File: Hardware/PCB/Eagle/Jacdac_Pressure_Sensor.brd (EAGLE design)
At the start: 27.9 x 27.9 mm, 29 parts, among them J1 JACDAC_EDGE_CONN-INNIE, J2 SWD-ADAPTER-, U1 NCP114ASN330T1G, U2 STM32F042F6P6, U3 LPS33HWTR, U4 BAT54S,235

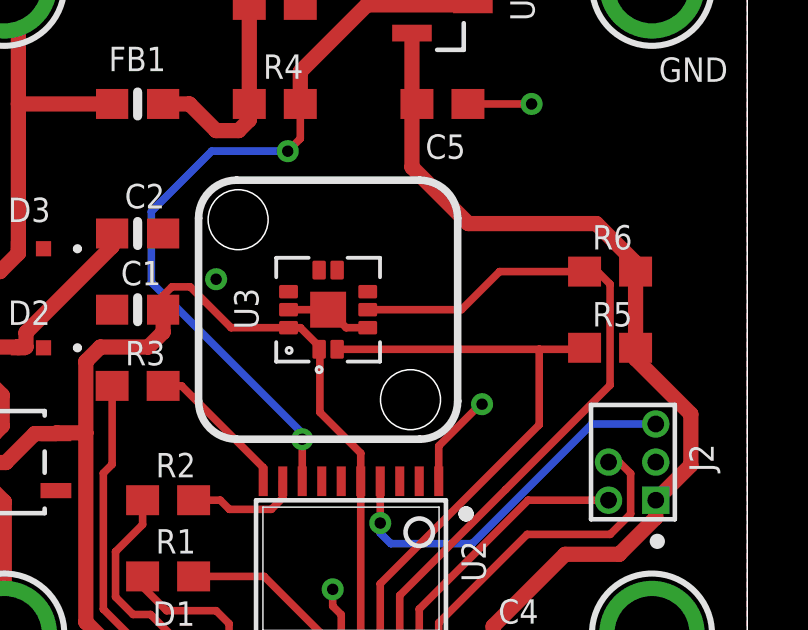
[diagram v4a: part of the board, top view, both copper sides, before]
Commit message: Added Additional ground via
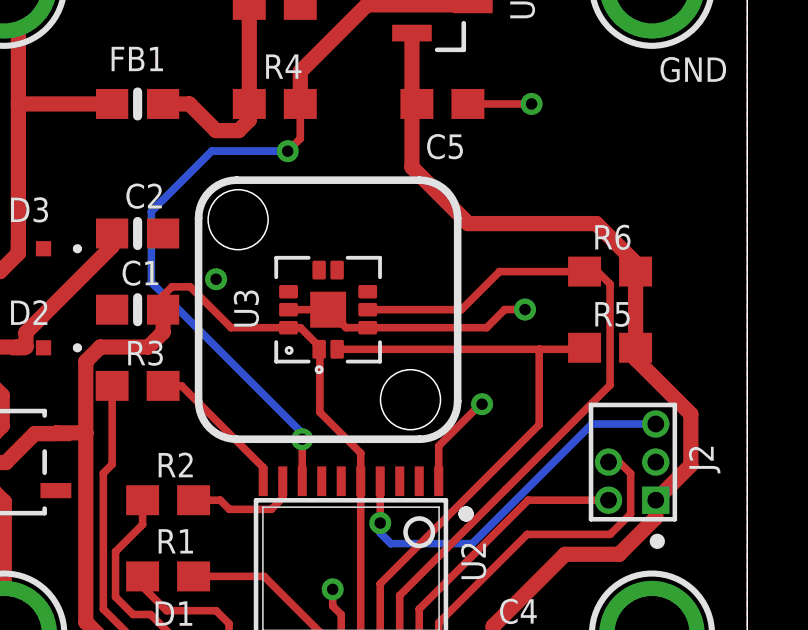
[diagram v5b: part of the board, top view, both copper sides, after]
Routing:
- net GND: track 15.9 -> 21.4 mm, vias 5 -> 6
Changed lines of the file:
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@@
 <drawing>
 <settings>
-<setting alwaysvectorfont="yes"/>
+<setting alwaysvectorfont="no"/>
 <setting keepoldvectorfont="yes"/>
 <setting verticaltext="up"/>
@@
 </layers>
 <board>
-<fusionsync huburn="a.cGVyc29uYWw6dWUyYWQxOTI2" projecturn="a.cGVyc29uYWw6dWUyYWQxOTI2IzIwMjEwOTEzNDQzNTc2ODA2" f3durn="urn:adsk.wipprod:dm.lineage:uby1OiGsR5OmPWsZuNtneA" pcbguid="" lastpulledtime="" lastsyncedchangeguid="" latestrevisionid="af606afd-fa91-40a1-9cdc-3a86e01ece8c" lastsyncedrevisionid="af606afd-fa91-40a1-9cdc-3a86e01ece8c" lastboardhashguid="dc86e965-abde-f830-b550-b611301090e1" lastpushedtime="2022-03-29T02:43:38Z" linktopcb3d="true"/>
+<fusionsync huburn="a.cGVyc29uYWw6dWUyYWQxOTI2" projecturn="a.cGVyc29uYWw6dWUyYWQxOTI2IzIwMjEwOTEzNDQzNTc2ODA2" f3durn="urn:adsk.wipprod:dm.lineage:uby1OiGsR5OmPWsZuNtneA" pcbguid="" lastpulledtime="" lastsyncedchangeguid="" latestrevisionid="1d99499d-ddfe-4265-9c5c-a70248ccb1e0" lastsyncedrevisionid="1d99499d-ddfe-4265-9c5c-a70248ccb1e0" lastboardhashguid="49f9fc46-0ca4-f778-ea88-d8f152bf949c" lastpushedtime="2022-03-30T00:31:33Z" linktopcb3d="true"/>
 <plain>
 <wire x1="2.54" y1="27.94" x2="25.4" y2="27.94" width="0.05" layer="20"/>
@@
 <contactref element="H3" pad="P$1"/>
 <contactref element="H4" pad="P$1"/>
+<via x="20.5333625" y="13.97508125" extent="1-16" drill="0.381"/>
+<wire x1="15.29" y1="13.37" x2="19.2526375" y2="13.37" width="0.254" layer="1"/>
+<wire x1="19.85771875" y1="13.97508125" x2="20.5333625" y2="13.97508125" width="0.254" layer="1"/>
+<wire x1="19.2526375" y1="13.37" x2="19.85771875" y2="13.97508125" width="0.254" layer="1"/>
 </signal>
 <signal name="VCC">
@@
 </signals>
 <mfgpreviewcolors>
-<mfgpreviewcolor name="soldermaskcolor" color="0xC8AA0000"/>
-<mfgpreviewcolor name="silkscreencolor" color="0xFFFEFEFE"/>
+<mfgpreviewcolor name="soldermaskcolor" color="0xC8D00003"/>
+<mfgpreviewcolor name="silkscreencolor" color="0xFFFFFFFF"/>
 <mfgpreviewcolor name="backgroundcolor" color="0xFF282828"/>
 <mfgpreviewcolor name="coppercolor" color="0xFFFFBF00"/>

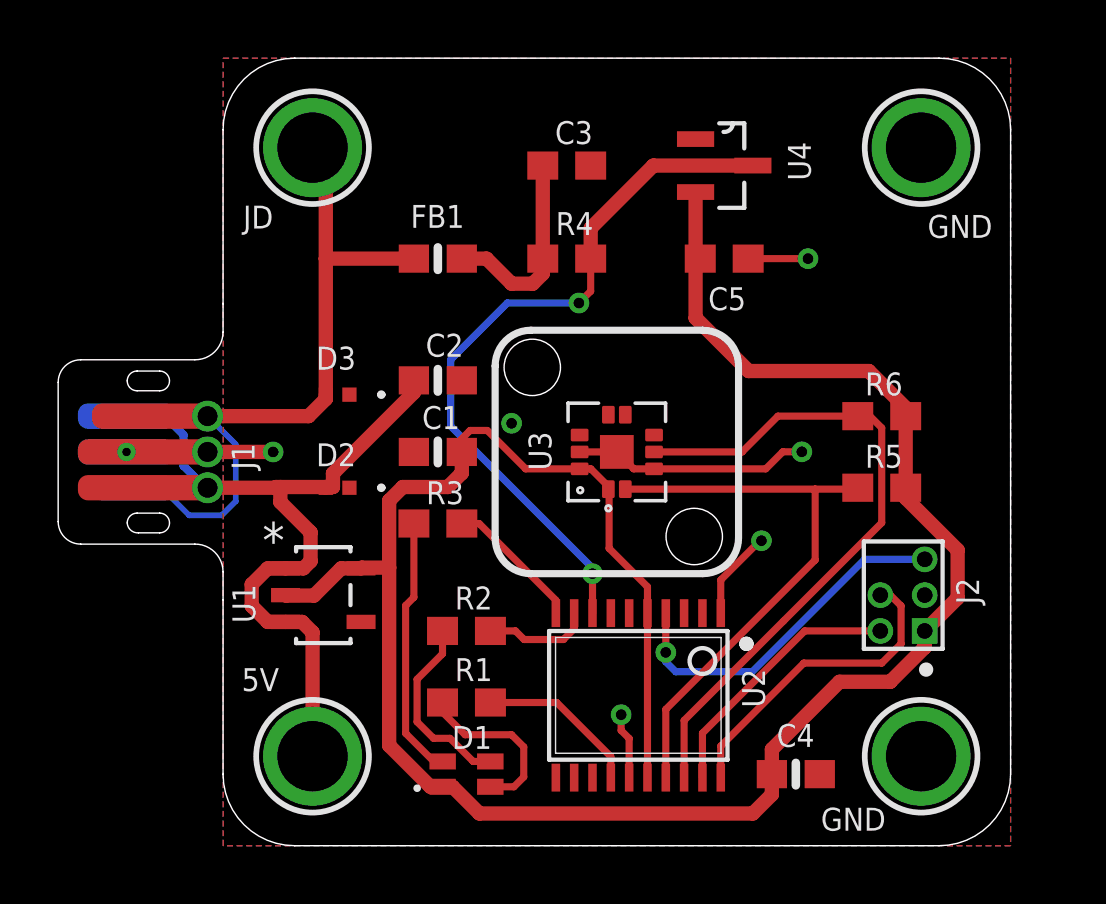
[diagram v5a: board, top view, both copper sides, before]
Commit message: Updated design : Centered Pressure Sensor
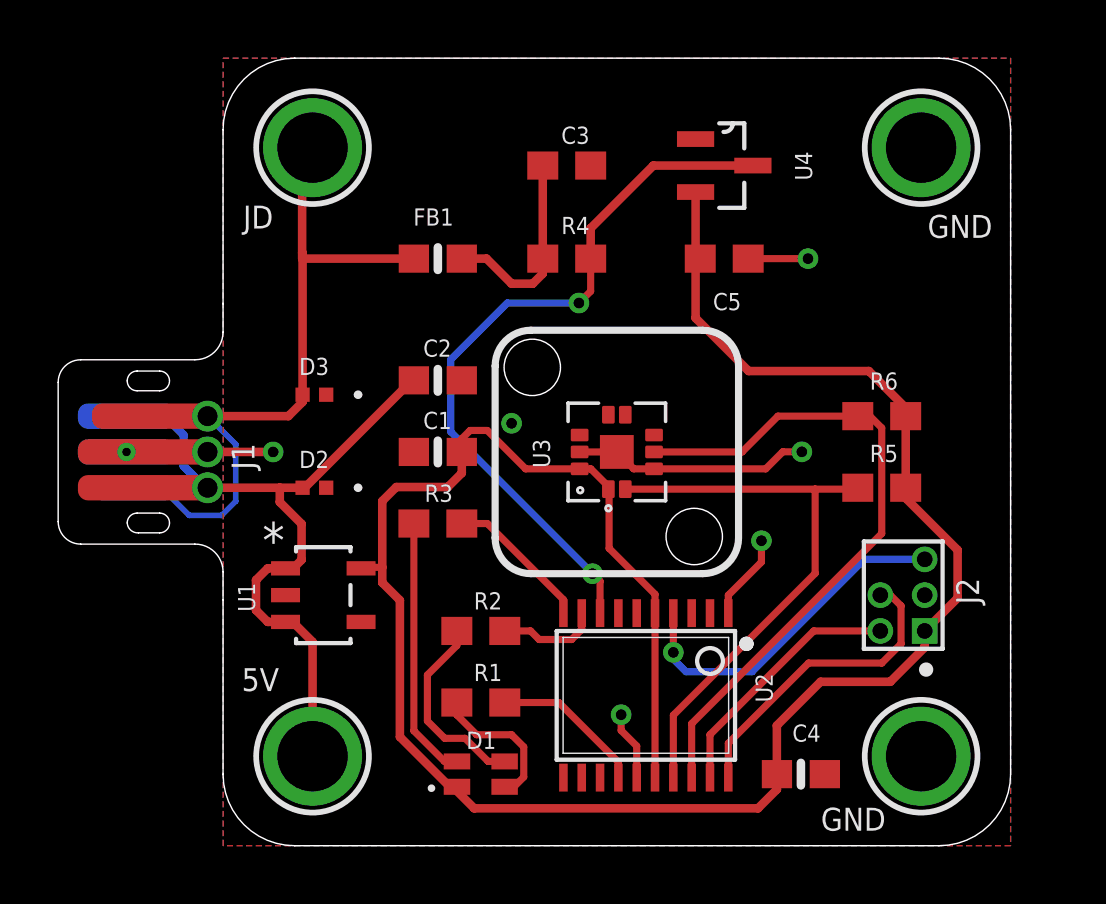
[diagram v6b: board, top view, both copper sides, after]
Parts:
- moved D3 0.82 mm to (3.24, 16.0)
- moved D2 0.82 mm to (3.24, 12.7)
- moved D1 0.51 mm to (9.14, 2.54)
- moved R1 0.51 mm to (9.14, 5.08)
- moved R2 0.51 mm to (9.14, 7.62)
- moved U2 0.27 mm to (15.0, 5.33)
- moved C4 0.18 mm to (20.5, 2.54)
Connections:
- net +3V3: no longer U1.2
- net GND: now also U1.2
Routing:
- net +3V3: track 80.6 -> 77.9 mm
- net VCC: track 29.5 -> 28.1 mm
- net N$1: track 6.13 -> 5.17 mm

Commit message: Added version 1.0
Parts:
- removed H1, H2, H3, H4: MOUNTINGHOLE2.5, milador:MOUNTINGHOLE_2.5_PLATED
- removed J1: JACDAC_EDGE_CONN-INNIE, Jacdac:JACDAC-EDGE-CONN-INNIE
- removed LABEL2: JACDAC-DEVICE-PS, milador:JACDAC-PRESSURE-SENSOR
- removed LABEL3: MILADOR-LOGO-, milador:MILADOR_LOGO1
- removed U$1: JACDAC-DEVICE-LPS33HW, milador:JACDAC-LPS33HW
- added J3: 5V, milador:M3-HOLE-PWR-OUTL
- added J4: DATA, milador:M3-HOLE-DATA-NOTCH
- added J5, J6: GND, milador:M3-HOLE-GND
- added JD1, JD2: JACDAC-EDGE-OUTIE, milador:JD-EDGE-OUTIE
- added LABEL_JACDAC_PS: MILADOR-JACDAC-DEVICE-PS, milador:JACDAC-PRESSURE-SENSOR
- added LABEL_LPS33HW: MILADOR-JACDAC-DEVICE-LPS33HW, milador:JACDAC-LPS33HW
- added LABEL_MILADOR: MILADOR-LOGO-, milador:MILADOR_LOGO1
- added LABEL_QR_CODE: MILADOR-QR-CODE-JACDAC-GITHUB-PS, milador:MILADOR_QR_JACDAC_PS
- C1: value 0.1uF -> 1uF
- C2: value 1uF -> 33pF; device milador_SMD:0603-NO -> milador_SMD:0603
- C3: value 33pF -> 1uF; device milador_SMD:0603 -> milador_SMD:0603-NO
- C4: value 1uF -> 0.1uF
- D1: value LED-HSMF-C114 -> DIODE-ZENER-AA-RCLAMP0521PATCT; device milador_SMD:DIOSC160X150X35-4N -> milador_SMD:DIODE-ZENER-0402
- D2: value RCLAMP0521PATCT -> DIODE-ZENER-AA-RCLAMP0521PATCT
- D3: value RCLAMP0521PATCT -> LED-HSMF-C114; device milador_SMD:DIODE-ZENER-0402 -> milador_SMD:DIOSC160X150X35-4N
- MMC_LOGO: value MMC_LOGO-SM -> MMC_LOGO-XSM; device MMC Eagle:MMC_SMALL_LOGO -> MMC Eagle:MMC_X-SMALL_LOGO
- U1: value NCP114ASN330T1G -> STM32F042F6P6; device milador_SMD:TSOP-5_ONS -> milador_SMD:TSSOP20
- U2: value STM32F042F6P6 -> NCP114ASN330T1G; device milador_SMD:TSSOP20 -> milador_SMD:TSOP-5_ONS
- moved C3 21.8 mm to (17.8, 3.00), turned to 270 degrees
- moved R1 12.1 mm to (9.80, 17.2)
- moved R2 12.1 mm to (9.80, 19.7)
- moved R3 11.0 mm to (9.80, 22.2)
- moved U1 10.1 mm to (12.8, 4.75), turned to 180 degrees
- moved MMC_LOGO 9.48 mm to (12.0, 4.50), turned to 0 degrees
- moved C4 9.13 mm to (18.8, 11.5)
- moved C1 8.49 mm to (8.25, 5.50), turned to 90 degrees
- moved U2 7.90 mm to (9.50, 11.0), turned to 90 degrees
- moved C2 7.42 mm to (14.0, 20.3)
- moved D1 7.28 mm to (7.00, 9.50), turned to 90 degrees
- moved FB1 6.55 mm to (13.8, 23.0)
- moved D3 6.24 mm to (9.30, 14.5), turned to 0 degrees
- moved R6 5.27 mm to (18.5, 17.2)
- moved J2 5.18 mm to (19.9, 6.25)
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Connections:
- net +3V3: now also C3.1, D3.1, U1.16; no longer C1.1, D1.1, U2.16
- net GND: now also D1.1, J5.H, J6.H, JD1.2, JD1.5, JD1.P$2, JD1.P$4, JD2.2, JD2.5, JD2.P$2, JD2.P$4, U1.1, U1.15, U2.2; no longer D3.1, H3.P$1, H4.P$1, J1.GND1, J1.GND2, J1.GND3, J1.GND4, U1.2, U2.1, U2.15
- net JD_DATA: now also U1.8; no longer U2.8
- net J_DATA: now also D2.2, J4.H, JD1.1, JD1.6, JD1.P$3, JD2.1, JD2.6, JD2.P$3; no longer D3.2, H2.P$1, J1.JD1, J1.JD2, J1.JD3
- net N$1: now also D3.4; no longer D1.4
- net N$2: now also D3.3; no longer D1.3
- net N$3: now also D3.2; no longer D1.2
- net N$4: now also C2.1; no longer C3.1
- net RESET: now also U1.4; no longer U2.4
- net RGB_B: now also U1.14; no longer U2.14
- net RGB_G: now also U1.10; no longer U2.9
- net RGB_R: now also U1.9; no longer U2.10
- net SCL: now also U1.17; no longer U2.17
- net SDA: now also U1.18; no longer U2.18
- net SWCLK: now also U1.20; no longer U2.20
- net SWDIO: now also U1.19; no longer U2.19
- net VCC: now also C1.1, D1.2, J3.H, JD1.3, JD1.4, JD1.P$1, JD2.3, JD2.4, JD2.P$1, U2.1, U2.3; no longer C2.1, D2.2, H1.P$1, J1.VDD1, J1.VDD2, J1.VDD3, U1.1, U1.3
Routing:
- net GND: track 21.4 -> 108.6 mm, vias 6 -> 10
- net +3V3: track 77.9 -> 47.4 mm, vias 0 -> 2
- net J_DATA: track 26.6 -> 51.4 mm, vias 0 -> 5
- net VCC: track 28.1 -> 48.9 mm
- net RGB_R: track 5.20 -> 21.0 mm, vias 0 -> 2
- net RGB_G: track 3.58 -> 17.4 mm, vias 0 -> 2
- net RGB_B: track 5.46 -> 17.7 mm, vias 0 -> 2
- net JD_DATA: track 26.1 -> 19.9 mm
- net RESET: track 12.4 -> 7.22 mm
- net SWCLK: track 11.0 -> 6.95 mm
- net SWDIO: track 9.09 -> 6.46 mm, vias 0 -> 1
- net SDA: track 24.0 -> 21.9 mm, vias 0 -> 2
- net SCL: track 20.6 -> 18.7 mm, vias 0 -> 2
- net N$4: track 7.22 -> 5.92 mm
- net N$3: track 9.33 -> 8.29 mm
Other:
- board size 27.9 x 27.9 mm -> 25 x 25 mm
- board text added: "V1.1"
- board text removed: "5V"
- board text removed: "JD"
